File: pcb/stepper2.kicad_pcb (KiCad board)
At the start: 2 copper layers, 210 x 120 mm, 18 parts, among them J1 DE15_Receptacle_HighDensity, J2 DE15_Receptacle_HighDensity, J3 DE15_Receptacle_HighDensity, SW1 SW_Push, SW2 SW_Push, SW3 SW_Push, SW4 SW_Push, SW5 SW_Push, SW6 SW_Push

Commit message: Nucleo footprint and updates on schematics
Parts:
- added U1: ~, stepper2:Nucleo144_H723, F.Cu at (250.4, 94.5)
- added U4: TMC2209_BIGTREETECH, stepper2:TMC2209_BIGTREETECH, F.Cu at (137.2, 43.2)
- added U5: TMC2209_BIGTREETECH, stepper2:TMC2209_BIGTREETECH, F.Cu at (156.2, 43.2)
- added U6: TMC2209_BIGTREETECH, stepper2:TMC2209_BIGTREETECH, F.Cu at (175.3, 43.2)
- C1, C2, C3: footprint Capacitor_SMD:C_0603_1608Metric -> Capacitor_SMD:C_1206_3216Metric_Pad1.33x1.80mm_HandSolder
- J1, J2, J3: footprint Connector_Dsub:DSUB-15-HD_Male_Horizontal_P2.29x2.54mm_EdgePinOffset9.40mm -> stepper2:DSUB-15-HD_Male_Horizontal_Pitch2.29x2.54mm_EdgePinOffset9.40mm
- R1, R2, R3: footprint Resistor_SMD:R_0603_1608Metric -> Resistor_SMD:R_1206_3216Metric_Pad1.30x1.75mm_HandSolder

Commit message: Basic layout of the PCB, encoder connectors added
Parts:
- added BT1: 3V, Battery:BatteryHolder_Keystone_1060_1x2032, F.Cu at (76.5, 116.3)
- added J4: DA15_Receptacle_MountingHoles, stepper2:DSUB-15-HD_Vertical_Pitch2.29x1.98mm_Mercury3000_Enc, F.Cu at (60.5, 13.5)
- added J5: DA15_Receptacle_MountingHoles, stepper2:DSUB-15-HD_Vertical_Pitch2.29x1.98mm_Mercury3000_Enc, F.Cu at (60.5, 43.0)
- added J6: DA15_Receptacle_MountingHoles, stepper2:DSUB-15-HD_Vertical_Pitch2.29x1.98mm_Mercury3000_Enc, F.Cu at (60.5, 72.0)
- added R10: 120R, Resistor_SMD:R_1206_3216Metric_Pad1.30x1.75mm_HandSolder, F.Cu at (50.9, 81.0)
- added R11: 120R, Resistor_SMD:R_1206_3216Metric_Pad1.30x1.75mm_HandSolder, F.Cu at (54.2, 81.0)
- added R12: 120R, Resistor_SMD:R_1206_3216Metric_Pad1.30x1.75mm_HandSolder, F.Cu at (57.5, 81.0)
- added R4: 120R, Resistor_SMD:R_1206_3216Metric_Pad1.30x1.75mm_HandSolder, F.Cu at (46.9, 57.5)
- added R5: 120R, Resistor_SMD:R_1206_3216Metric_Pad1.30x1.75mm_HandSolder, F.Cu at (50.2, 57.5)
- added R6: 120R, Resistor_SMD:R_1206_3216Metric_Pad1.30x1.75mm_HandSolder, F.Cu at (53.5, 57.5)
- added R7: 120R, Resistor_SMD:R_1206_3216Metric_Pad1.30x1.75mm_HandSolder, F.Cu at (55.6, 29.0)
- added R8: 120R, Resistor_SMD:R_1206_3216Metric_Pad1.30x1.75mm_HandSolder, F.Cu at (52.3, 29.0)
- added R9: 120R, Resistor_SMD:R_1206_3216Metric_Pad1.30x1.75mm_HandSolder, F.Cu at (49.0, 29.0)
- added U7: AM26LS32Ax, stepper2:SO-16_3.9x9.9mm_P1.27mm, F.Cu at (66.4, 57.5)
- added U8: AM26LS32ACN, stepper2:SO-16_3.9x9.9mm_P1.27mm, F.Cu at (66.9, 28.9)
- added U9: AM26LS32ACN, stepper2:SO-16_3.9x9.9mm_P1.27mm, F.Cu at (68.1, 86.1)
- J1, J2, J3: footprint stepper2:DSUB-15-HD_Male_Horizontal_Pitch2.29x2.54mm_EdgePinOffset9.40mm -> stepper2:DSUB-15-HD_Horizontal_Pitch2.29x2.54mm_EdgePinOffset9.40mm
- moved U1 195.8 mm to (55.9, 72.2), turned to 180 degrees
- moved U3 170.3 mm to (29.6, 114.2), turned to -90 degrees
- moved U6 160.7 mm to (21.5, 90.0)
- moved U5 137.3 mm to (21.5, 69.5)
- moved U4 115.8 mm to (21.5, 49.0)
- moved SW5 110.2 mm to (17.0, 27.0), turned to 90 degrees
- moved U2 108.6 mm to (54.5, 122.5), turned to 180 degrees
- moved SW3 107.4 mm to (17.0, 17.0), turned to 90 degrees
- moved SW6 106.8 mm to (27.0, 27.0), turned to 90 degrees
- moved SW1 104.8 mm to (17.0, 7.00), turned to 90 degrees
- moved SW4 103.5 mm to (27.0, 17.0), turned to 90 degrees
- moved SW2 100.4 mm to (27.0, 7.00), turned to 90 degrees
- moved C1 81.1 mm to (39.9, 55.0)
- moved C2 81.1 mm to (39.9, 57.5)
- moved C3 81.1 mm to (39.9, 60.0)
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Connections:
- POWER_5V1 pad 1: unconnected-(POWER_5V1-Pad1) -> VCC
- POWER_5V1 pad 2: unconnected-(POWER_5V1-Pad2) -> GND
- SW1 pad 2: unconnected-(SW1-Pad2) -> GND
- SW2 pad 2: unconnected-(SW2-Pad2) -> GND
- SW3 pad 2: unconnected-(SW3-Pad2) -> GND
- SW4 pad 2: unconnected-(SW4-Pad2) -> GND
- SW5 pad 2: unconnected-(SW5-Pad2) -> GND
- SW6 pad 2: unconnected-(SW6-Pad2) -> GND
- U1 pad A11: unconnected-(U1A-GND-PadA11) -> GND
- U1 pad A13: unconnected-(U1A-GND-PadA13) -> GND
- U1 pad A28: unconnected-(U1A-GND-PadA28) -> GND
- U1 pad A39: unconnected-(U1A-GND-PadA39) -> GND
- U1 pad A7: unconnected-(U1A-3V3-PadA7) -> +3V3
- U1 pad A9: unconnected-(U1A-5V-PadA9) -> +5V
- U1 pad B23: unconnected-(U1B-GND-PadB23) -> GND
- U1 pad B25: unconnected-(U1B-GND-PadB25) -> GND
- U1 pad B37: unconnected-(U1B-GND-PadB37) -> GND
- U1 pad B42: unconnected-(U1B-GND-PadB42) -> GND
- U1 pad B47: unconnected-(U1B-GND-PadB47) -> GND
- U1 pad B8: unconnected-(U1B-GND-PadB8) -> GND
- U2 pad 8: unconnected-(U2-VCCIO-Pad8) -> Net-(U2-3V3)
- U2 pad 9: unconnected-(U2-3V3-Pad9) -> Net-(U2-3V3)
- U3 pad 2: unconnected-(U3-IN+-Pad2) -> VCC
- U3 pad 4: unconnected-(U3-OUT+-Pad4) -> +5V
- U4 pad 1: unconnected-(U4-GND-Pad1) -> GND
- U4 pad 11: unconnected-(U4-!EN-Pad11) -> GND
- U4 pad 2: unconnected-(U4-VIO-Pad2) -> +3V3
- U4 pad 7: unconnected-(U4-GND-Pad7) -> GND
- U4 pad 8: unconnected-(U4-VM-Pad8) -> VCC
- U5 pad 1: unconnected-(U5-GND-Pad1) -> GND
- U5 pad 2: unconnected-(U5-VIO-Pad2) -> +3V3
- U5 pad 7: unconnected-(U5-GND-Pad7) -> GND
- U5 pad 8: unconnected-(U5-VM-Pad8) -> VCC
- U6 pad 1: unconnected-(U6-GND-Pad1) -> GND
- U6 pad 2: unconnected-(U6-VIO-Pad2) -> +3V3
- U6 pad 7: unconnected-(U6-GND-Pad7) -> GND
- U6 pad 8: unconnected-(U6-VM-Pad8) -> VCC
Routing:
- removed copper zone on B.Cu, net GND
- removed copper zone on F.Cu, net GND
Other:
- board size 210 x 120 mm -> 91.5 x 138 mm

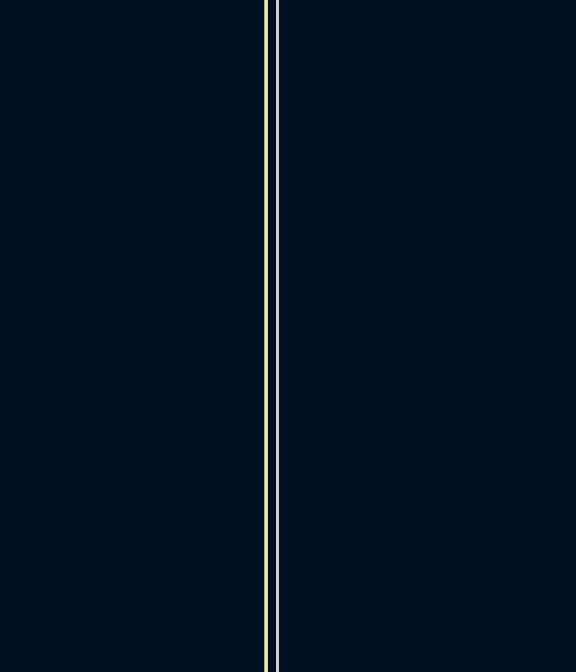
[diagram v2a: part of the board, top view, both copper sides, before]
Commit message: added 4, 5, 6, 7 pin JST connectors
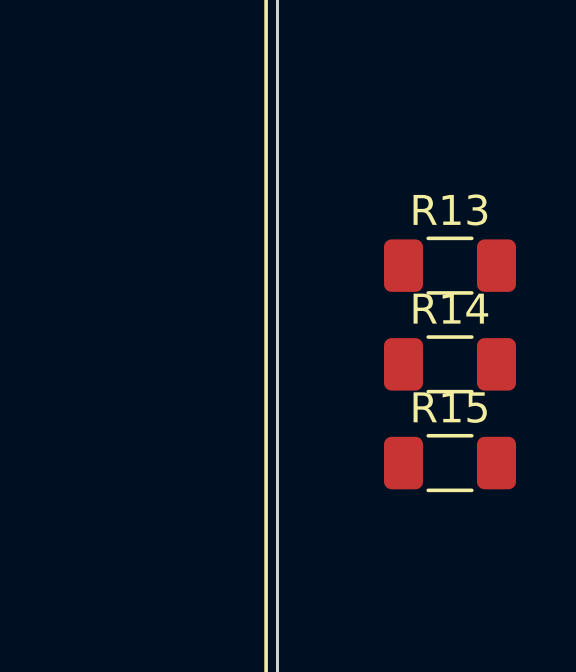
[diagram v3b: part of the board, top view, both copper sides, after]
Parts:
- added R13: 1k, Resistor_SMD:R_1206_3216Metric_Pad1.30x1.75mm_HandSolder, F.Cu at (97.2, 50.8)
- added R14: 1k, Resistor_SMD:R_1206_3216Metric_Pad1.30x1.75mm_HandSolder, F.Cu at (97.2, 54.1)
- added R15: 1k, Resistor_SMD:R_1206_3216Metric_Pad1.30x1.75mm_HandSolder, F.Cu at (97.2, 57.4)
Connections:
- C1 pad 1: Net-(C1-Pad1) -> VREF1
- C2 pad 1: Net-(C2-Pad1) -> VREF2
- C3 pad 1: Net-(C3-Pad1) -> VREF3
- J1 pad 1: unconnected-(J1-Pad1) -> GND
- J1 pad 13: unconnected-(J1-Pad13) -> +5V
- J1 pad 15: unconnected-(J1-Pad15) -> GND
- J1 pad 2: unconnected-(J1-Pad2) -> FLIMIT1
- J1 pad 3: unconnected-(J1-Pad3) -> RLIMIT1
- J1 pad 4: unconnected-(J1-Pad4) -> MYA1
- J1 pad 5: unconnected-(J1-Pad5) -> MYB1
- J1 pad 6: unconnected-(J1-Pad6) -> MXA1
- J1 pad 7: unconnected-(J1-Pad7) -> MYA1
- J2 pad 1: unconnected-(J2-Pad1) -> GND
- J2 pad 13: unconnected-(J2-Pad13) -> +5V
- J2 pad 15: unconnected-(J2-Pad15) -> GND
- J2 pad 2: unconnected-(J2-Pad2) -> FLIMIT2
- J2 pad 3: unconnected-(J2-Pad3) -> RLIMIT2
- J2 pad 4: unconnected-(J2-Pad4) -> MYA2
- J2 pad 5: unconnected-(J2-Pad5) -> MYB2
- J2 pad 6: unconnected-(J2-Pad6) -> MXA2
- J2 pad 7: unconnected-(J2-Pad7) -> MYA2
- J3 pad 1: unconnected-(J3-Pad1) -> GND
- J3 pad 13: unconnected-(J3-Pad13) -> +5V
- J3 pad 15: unconnected-(J3-Pad15) -> GND
- J3 pad 2: unconnected-(J3-Pad2) -> FLIMIT3
- J3 pad 3: unconnected-(J3-Pad3) -> RLIMIT3
- J3 pad 4: unconnected-(J3-Pad4) -> MYA3
- J3 pad 5: unconnected-(J3-Pad5) -> MYB3
- J3 pad 6: unconnected-(J3-Pad6) -> MXA3
- J3 pad 7: unconnected-(J3-Pad7) -> MYA3
- J4 pad 10: unconnected-(J4-P10-Pad10) -> ENCB1+
- J4 pad 12: unconnected-(J4-P12-Pad12) -> +5V
- J4 pad 13: unconnected-(J4-P13-Pad13) -> GND
- J4 pad 14: unconnected-(J4-P14-Pad14) -> ENCI1+
- J4 pad 15: unconnected-(J4-P15-Pad15) -> ENCI1-
- J4 pad 4: unconnected-(J4-Pad4) -> ENCA1-
- J4 pad 5: unconnected-(J4-Pad5) -> ENCA1+
- J4 pad 9: unconnected-(J4-P9-Pad9) -> ENCB1-
- J5 pad 10: unconnected-(J5-P10-Pad10) -> ENCB2+
- J5 pad 12: unconnected-(J5-P12-Pad12) -> +5V
- J5 pad 13: unconnected-(J5-P13-Pad13) -> GND
- J5 pad 14: unconnected-(J5-P14-Pad14) -> ENCI2+
- J5 pad 15: unconnected-(J5-P15-Pad15) -> ENCI2-
- J5 pad 4: unconnected-(J5-Pad4) -> ENCA2-
- J5 pad 5: unconnected-(J5-Pad5) -> ENCA2+
- J5 pad 9: unconnected-(J5-P9-Pad9) -> ENCB2-
- J6 pad 10: unconnected-(J6-P10-Pad10) -> ENCB3+
- J6 pad 12: unconnected-(J6-P12-Pad12) -> +5V
- J6 pad 13: unconnected-(J6-P13-Pad13) -> GND
- J6 pad 14: unconnected-(J6-P14-Pad14) -> ENCI3+
- J6 pad 15: unconnected-(J6-P15-Pad15) -> ENCI3-
- J6 pad 4: unconnected-(J6-Pad4) -> ENCA3-
- J6 pad 5: unconnected-(J6-Pad5) -> ENCA3+
- J6 pad 9: unconnected-(J6-P9-Pad9) -> ENCB3-
- R1 pad 1: Net-(C1-Pad1) -> VREF1
- R1 pad 2: VREF1 -> VREFPWM1
- R10 pad 1: Net-(U9-2A) -> ENCB3+
- R10 pad 2: Net-(U9-2B) -> ENCB3-
- R11 pad 1: Net-(U9-3A) -> ENCI3+
- R11 pad 2: Net-(U9-3B) -> ENCI3-
- R12 pad 1: Net-(U9-1A) -> ENCA3+
- R12 pad 2: Net-(U9-1B) -> ENCA3-
- R2 pad 1: Net-(C2-Pad1) -> VREF2
- R2 pad 2: VREF1 -> VREFPWM2
- R3 pad 1: Net-(C3-Pad1) -> VREF3
- R3 pad 2: VREF1 -> VREFPWM3
- R4 pad 1: Net-(U7-1A) -> ENCA2+
- R4 pad 2: Net-(U7-1B) -> ENCA2-
- R5 pad 1: Net-(U7-2A) -> ENCB2+
- R5 pad 2: Net-(U7-2B) -> ENCB2-
- R6 pad 1: Net-(U7-3A) -> ENCI2+
- R6 pad 2: Net-(U7-3B) -> ENCI2-
- R7 pad 1: Net-(U8-2A) -> ENCB1+
- R7 pad 2: Net-(U8-2B) -> ENCB1-
- R8 pad 1: Net-(U8-3A) -> ENCI1+
- R8 pad 2: Net-(U8-3B) -> ENCI1-
- R9 pad 1: Net-(U8-1A) -> ENCA1+
- R9 pad 2: Net-(U8-1B) -> ENCA1-
- U1 pad A10: unconnected-(U1A-PC12-PadA10) -> Net-(U1A-PC12)
- U1 pad A12: unconnected-(U1A-PD2-PadA12) -> TMCUART2
- U1 pad A20: unconnected-(U1A-PD6-PadA20) -> USBUARTRX
- U1 pad A22: unconnected-(U1A-PD5-PadA22) -> USBUARTTX
- U1 pad A6: unconnected-(U1A-PC10-PadA6) -> Net-(U1A-PC10)
- U1 pad A8: unconnected-(U1A-PC11-PadA8) -> TMCUART3
- U1 pad B1: unconnected-(U1B-PC6-PadB1) -> ENCA3
- U1 pad B10: unconnected-(U1B-PA5-PadB10) -> NXT3
- U1 pad B11: unconnected-(U1B-PC7-PadB11) -> ENCB3
- U1 pad B12: unconnected-(U1B-PA6-PadB12) -> ENCA2
- U1 pad B14: unconnected-(U1B-PB5-PadB14) -> ENCB2
- U1 pad B16: unconnected-(U1B-PD14-PadB16) -> ENCI2
- U1 pad B2: unconnected-(U1B-PB8-PadB2) -> DIAG3
- U1 pad B22: unconnected-(U1B-PG12-PadB22) -> NXT2
- U1 pad B24: unconnected-(U1B-PE9-PadB24) -> VREFPWM1
- U1 pad B26: unconnected-(U1B-PE11-PadB26) -> VREFPWM2
- U1 pad B3: unconnected-(U1B-PB15-PadB3) -> ENCI3
- U1 pad B30: unconnected-(U1B-PE13-PadB30) -> VREFPWM3
- U1 pad B34: unconnected-(U1B-PB6-PadB34) -> DIAG2
- U1 pad B36: unconnected-(U1B-PB7-PadB36) -> DIAG1
- U1 pad B38: unconnected-(U1B-PE8-PadB38) -> Net-(U1B-PE8)
- U1 pad B39: unconnected-(U1B-PD13-PadB39) -> ENCB1
- U1 pad B40: unconnected-(U1B-PE7-PadB40) -> TMCUART1
- U1 pad B41: unconnected-(U1B-PD12-PadB41) -> ENCA1
- U1 pad B43: unconnected-(U1B-PD11-PadB43) -> ENCI1
- U1 pad B49: unconnected-(U1B-PA0-PadB49) -> NXT1
- U1 pad B54: unconnected-(U1B-PB11-PadB54) -> DIAG1
- U2 pad 3: unconnected-(U2-TXD-Pad3) -> USBUARTRX
- U2 pad 4: unconnected-(U2-RXD-Pad4) -> USBUARTTX
- U4 pad 10: unconnected-(U4-VREF-Pad10) -> VREF1
- U4 pad 11: GND -> EN1
- U4 pad 12: unconnected-(U4-MS1-Pad12) -> GND
- U4 pad 13: unconnected-(U4-MS2-Pad13) -> +3V3
- U4 pad 14: unconnected-(U4-UART/RX-Pad14) -> TMCUART1
- U4 pad 17: unconnected-(U4-STEP-Pad17) -> NXT1
- U4 pad 18: unconnected-(U4-DIR-Pad18) -> DIR1
- U4 pad 3: unconnected-(U4-M1B-Pad3) -> MXB1
- U4 pad 4: unconnected-(U4-M1A-Pad4) -> MXA1
- U4 pad 5: unconnected-(U4-M2A-Pad5) -> MYA1
- U4 pad 6: unconnected-(U4-M2B-Pad6) -> MYB1
- U4 pad 9: unconnected-(U4-DIAG-Pad9) -> DIAG1
- U5 pad 10: unconnected-(U5-VREF-Pad10) -> VREF2
- U5 pad 11: unconnected-(U5-!EN-Pad11) -> EN2
- U5 pad 12: unconnected-(U5-MS1-Pad12) -> GND
- U5 pad 13: unconnected-(U5-MS2-Pad13) -> +3V3
- U5 pad 14: unconnected-(U5-UART/RX-Pad14) -> TMCUART2
- U5 pad 17: unconnected-(U5-STEP-Pad17) -> NXT2
- U5 pad 18: unconnected-(U5-DIR-Pad18) -> DIR2
- U5 pad 3: unconnected-(U5-M1B-Pad3) -> MXB2
- U5 pad 4: unconnected-(U5-M1A-Pad4) -> MXA2
- U5 pad 5: unconnected-(U5-M2A-Pad5) -> MYA2
- U5 pad 6: unconnected-(U5-M2B-Pad6) -> MYB2
- U5 pad 9: unconnected-(U5-DIAG-Pad9) -> DIAG2
- U6 pad 10: unconnected-(U6-VREF-Pad10) -> VREF3
- U6 pad 11: unconnected-(U6-!EN-Pad11) -> EN3
- U6 pad 12: unconnected-(U6-MS1-Pad12) -> GND
- U6 pad 13: unconnected-(U6-MS2-Pad13) -> +3V3
- U6 pad 14: unconnected-(U6-UART/RX-Pad14) -> TMCUART3
- U6 pad 17: unconnected-(U6-STEP-Pad17) -> NXT3
- U6 pad 18: unconnected-(U6-DIR-Pad18) -> DIR3
- U6 pad 3: unconnected-(U6-M1B-Pad3) -> MXB3
- U6 pad 4: unconnected-(U6-M1A-Pad4) -> MXA3
- U6 pad 5: unconnected-(U6-M2A-Pad5) -> MYA3
- U6 pad 6: unconnected-(U6-M2B-Pad6) -> MYB3
- U6 pad 9: unconnected-(U6-DIAG-Pad9) -> DIAG3
- U7 pad 1: Net-(U7-1B) -> ENCA2-
- U7 pad 10: Net-(U7-3A) -> ENCI2+
- U7 pad 2: Net-(U7-1A) -> ENCA2+
- U7 pad 6: Net-(U7-2A) -> ENCB2+
- U7 pad 7: Net-(U7-2B) -> ENCB2-
- U7 pad 9: Net-(U7-3B) -> ENCI2-
- U8 pad 1: Net-(U8-1B) -> ENCA1-
- U8 pad 10: Net-(U8-3A) -> ENCI1+
- U8 pad 2: Net-(U8-1A) -> ENCA1+
- U8 pad 6: Net-(U8-2A) -> ENCB1+
- U8 pad 7: Net-(U8-2B) -> ENCB1-
- U8 pad 9: Net-(U8-3B) -> ENCI1-
- U9 pad 1: Net-(U9-1B) -> ENCA3-
- U9 pad 10: Net-(U9-3A) -> ENCI3+
- U9 pad 2: Net-(U9-1A) -> ENCA3+
- U9 pad 6: Net-(U9-2A) -> ENCB3+
- U9 pad 7: Net-(U9-2B) -> ENCB3-
- U9 pad 9: Net-(U9-3B) -> ENCI3-

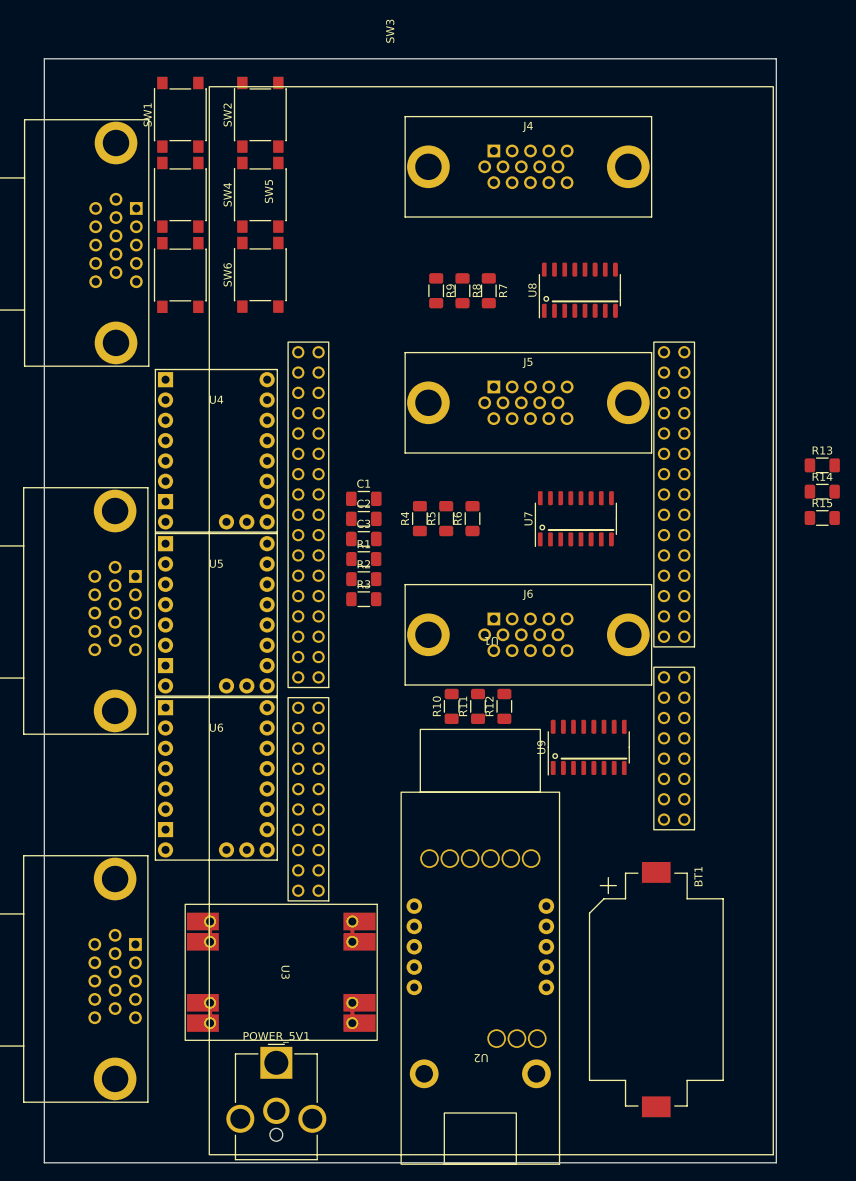
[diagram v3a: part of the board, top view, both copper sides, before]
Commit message: PCB - added VBAT; JST peripherial connectors; power supply capacitors
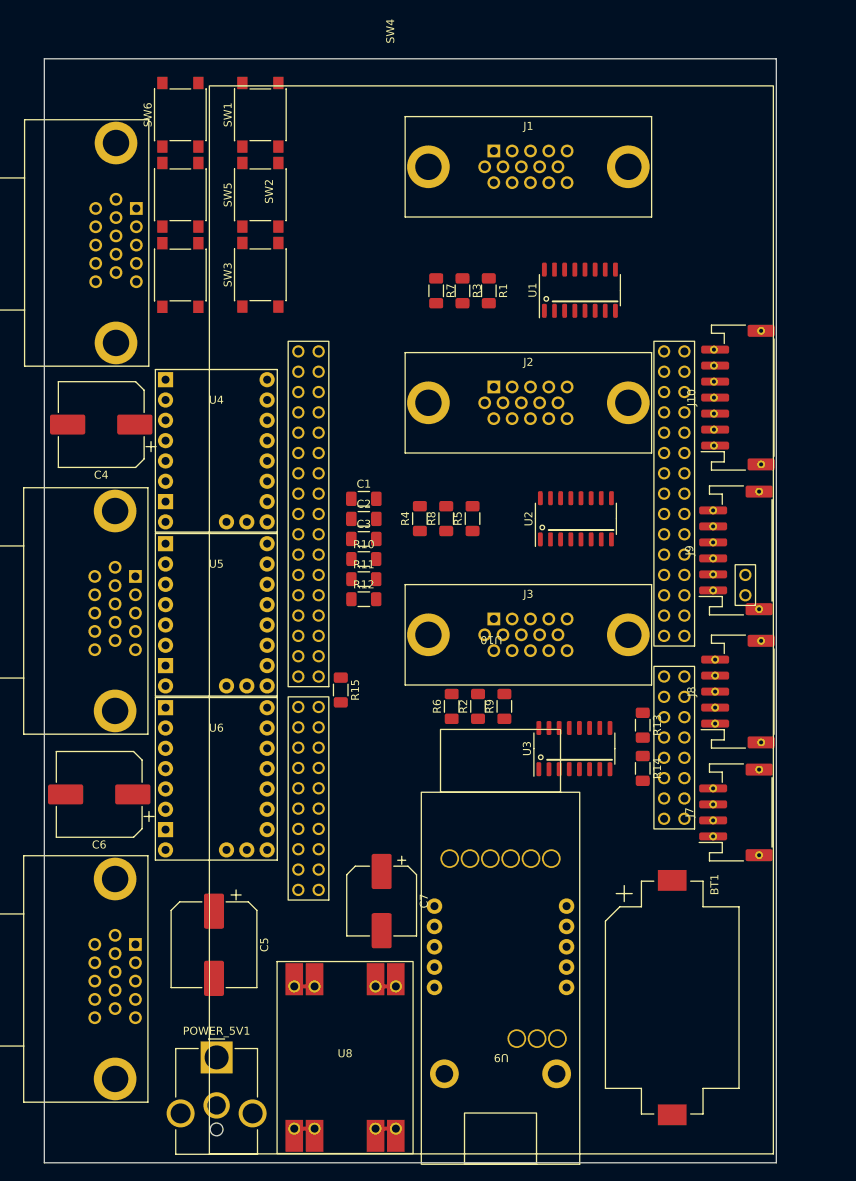
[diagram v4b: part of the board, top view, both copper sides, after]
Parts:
- removed the U1 at (55.9, 72.2)
- added C4: C_Polarized, Capacitor_SMD:CP_Elec_10x10.5, F.Cu at (7.11, 45.7)
- added C5: C_Polarized, Capacitor_SMD:CP_Elec_10x10.5, F.Cu at (21.2, 110.7)
- added C6: C_Polarized, Capacitor_SMD:CP_Elec_10x10.5, F.Cu at (6.86, 91.9)
- added C7: C_Polarized, Capacitor_SMD:CP_Elec_8x10.5, F.Cu at (42.2, 105.3)
- added J10: Conn_01x07_Pin, stepper2:JST_PH_S7B-PH-SM4-TB_1x07-1MP_P2.00mm_Horizontal, F.Cu at (86.7, 42.4)
- added J7: Conn_01x04_Pin, stepper2:JST_PH_S4B-PH-SM4-TB_1x04-1MP_P2.00mm_Horizontal, F.Cu at (86.5, 94.2)
- added J8: Conn_01x05_Pin, stepper2:JST_PH_S5B-PH-SM4-TB_1x05-1MP_P2.00mm_Horizontal, F.Cu at (86.7, 79.1)
- added J9: Conn_01x06_Pin, stepper2:JST_PH_S6B-PH-SM4-TB_1x06-1MP_P2.00mm_Horizontal, F.Cu at (86.5, 61.5)
- added U10: ~, stepper2:Nucleo144_H723_withVBAT, F.Cu at (55.9, 72.1)
- moved R15 63.9 mm to (37.0, 78.9), turned to -90 degrees
- moved R14 44.0 mm to (74.8, 88.7), turned to -90 degrees
- moved R13 36.8 mm to (74.8, 83.3), turned to -90 degrees
- moved U8 13.3 mm to (37.6, 124.8), turned to 0 degrees
- moved POWER_5V1 7.50 mm to (21.5, 124.8)
- moved U9 2.52 mm to (57.0, 122.5)
- moved BT1 2.22 mm to (78.5, 117.3)
- moved U3 1.81 mm to (66.3, 86.2)
- renumbered J4 to J1, J5 to J2, J6 to J3, J1 to J4, J2 to J5, J3 to J6, R7 to R1, R1 to R10, R2 to R11, R3 to R12, R14 to R13, R13 to R14, R11 to R2, R8 to R3, R6 to R5, R10 to R6, R9 to R7, R5 to R8, R12 to R9, SW2 to SW1, SW5 to SW2, SW6 to SW3, SW3 to SW4, SW4 to SW5, SW1 to SW6, U8 to U1, U7 to U2, U9 to U3, U3 to U8, U2 to U9
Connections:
- R13 pad 2: Net-(U1A-PC12) -> TMCUARTTX2
- R14 pad 2: Net-(U1A-PC10) -> TMCUARTTX3
- R15 pad 2: Net-(U1B-PE8) -> TMCUARTTX1
- SW1 pad 1: unconnected-(SW2-Pad1) -> UP1
- SW2 pad 1: unconnected-(SW5-Pad1) -> UP2
- SW3 pad 1: unconnected-(SW6-Pad1) -> UP3
- SW4 pad 1: unconnected-(SW3-Pad1) -> DOWN1
- SW5 pad 1: unconnected-(SW4-Pad1) -> DOWN2
- SW6 pad 1: unconnected-(SW1-Pad1) -> DOWN3
